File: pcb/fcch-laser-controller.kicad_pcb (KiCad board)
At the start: 2 copper layers, 90 x 80 mm, 31 parts, among them J1 Barrel_Jack_Switch, J10 Conn_01x03_Male, J11 Conn_01x02_Male, J12 Conn_01x04_Male, J13 Conn_01x19_Male, J14 Conn_01x19_Male, J2 Barrel_Jack_Switch, J3 Barrel_Jack_Switch, J4 Barrel_Jack_Switch, J5 Conn_02x03_Odd_Even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

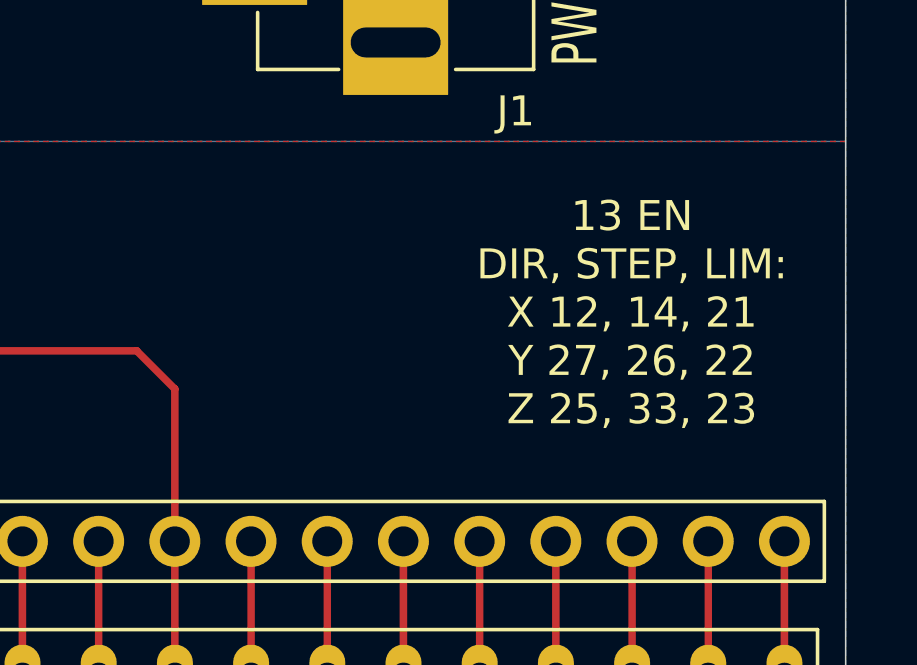
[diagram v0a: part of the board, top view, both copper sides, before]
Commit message: pcb: enhance PCB silk, add TODO entry
- Document the LASER and air control GPIO numbers.
- Note that the transistor footprint may need to be changed.
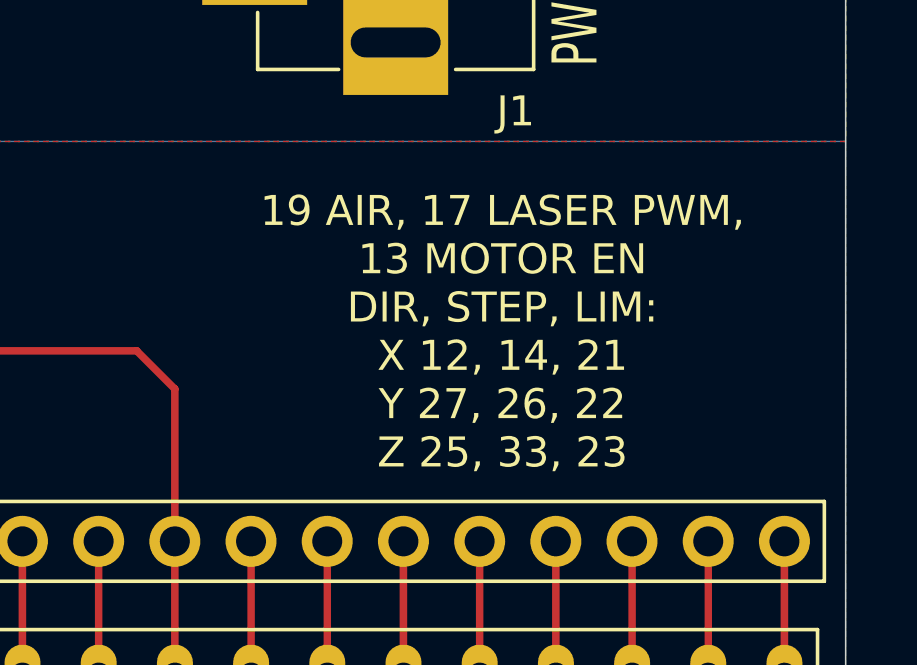
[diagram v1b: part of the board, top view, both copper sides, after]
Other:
- board text added: "19 AIR, 17 LASER PWM, 13 MOTOR EN DIR, STEP, LIM: X 12, 14, 21 Y 27, 26, 22 Z 25, 33, 23"
- board text removed: "13 EN DIR, STEP, LIM: X 12, 14, 21 Y 27, 26, 22 Z 25, 33, 23"
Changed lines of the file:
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@@
     )
   )
-  (gr_text "13 EN\nDIR, STEP, LIM:\nX 12, 14, 21\nY 27, 26, 22\nZ 25, 33, 23" (at 182.88 92.71) (layer F.SilkS)
+  (gr_text "19 AIR, 17 LASER PWM,\n13 MOTOR EN\nDIR, STEP, LIM:\nX 12, 14, 21\nY 27, 26, 22\nZ 25, 33, 23" (at 178.562 93.345) (layer F.SilkS)
     (effects (font (size 1 1) (thickness 0.15)))
   )
